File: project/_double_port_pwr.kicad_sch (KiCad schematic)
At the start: 8 parts, among them J201 RJ45_LED_Shielded_x2, U201 PCA9685PW

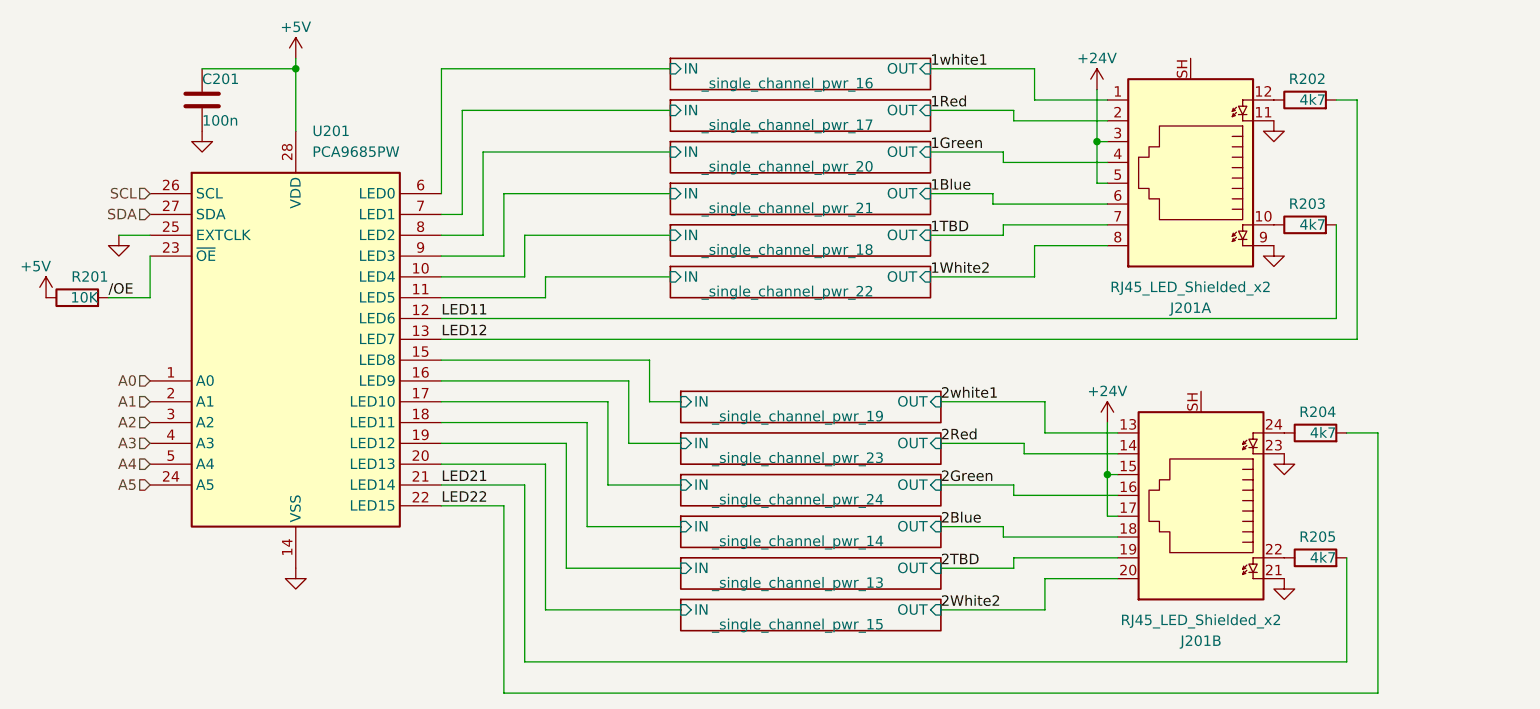
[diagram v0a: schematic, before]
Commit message: 2ch grouping layout
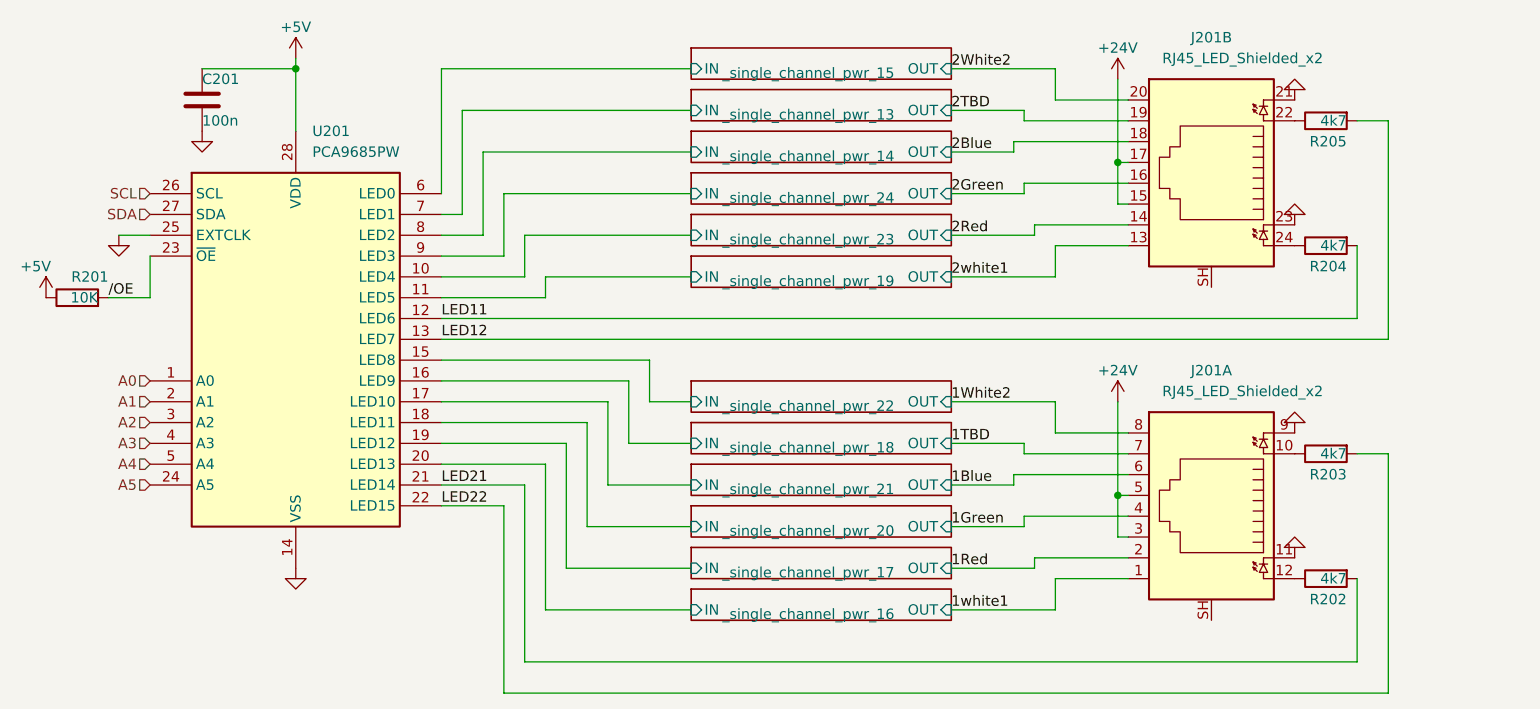
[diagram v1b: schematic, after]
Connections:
- net LED11: now also R204.2; no longer R203.2
- net LED12: now also R205.2; no longer R202.2
- net LED21: now also R202.2; no longer R205.2
- net LED22: now also R203.2; no longer R204.2
- net _single_channel_pwr_13/IN: now also U201.7 (LED1); no longer U201.19 (LED12)
- net _single_channel_pwr_14/IN: now also U201.8 (LED2); no longer U201.18 (LED11)
- net _single_channel_pwr_15/IN: now also U201.6 (LED0); no longer U201.20 (LED13)
- net _single_channel_pwr_16/IN: now also U201.20 (LED13); no longer U201.6 (LED0)
- net _single_channel_pwr_17/IN: now also U201.19 (LED12); no longer U201.7 (LED1)
- net _single_channel_pwr_18/IN: now also U201.16 (LED9); no longer U201.10 (LED4)
- net _single_channel_pwr_19/IN: now also U201.11 (LED5); no longer U201.15 (LED8)
- net _single_channel_pwr_20/IN: now also U201.18 (LED11); no longer U201.8 (LED2)
- net _single_channel_pwr_21/IN: now also U201.17 (LED10); no longer U201.9 (LED3)
- net _single_channel_pwr_22/IN: now also U201.15 (LED8); no longer U201.11 (LED5)
- net _single_channel_pwr_23/IN: now also U201.10 (LED4); no longer U201.16 (LED9)
- net _single_channel_pwr_24/IN: now also U201.9 (LED3); no longer U201.17 (LED10)
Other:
- moved on the sheet: J201A, J201B, R202, R203, R204, R205

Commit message: more layout
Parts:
- renumbered C201 to C12, J201 to J5, R204 to R10, R203 to R11, R202 to R12, R201 to R8, R205 to R9, U201 to U2
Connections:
- net GND: now also J5.SH, J5.SH
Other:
- title: (none) -> LED Dimmer 6x6
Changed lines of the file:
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@@
 (kicad_sch (version 20211123) (generator eeschema)
   (paper "A4")
+  (title_block
+    (title "LED Dimmer 6x6")
+    (date "2025-01-13")
+    (rev "1.0")
+  )
   (junction (at 191.77 118.11) (diameter 0) (color 0 0 0 0)
   )
@@
   (symbol (lib_id "-pwr:GND") (at 213.36 110.49 0) (mirror x) (unit 1)
     (in_bom yes) (on_board yes) (fields_autoplaced)
-    (property "Reference" "#PWR0209" (id 0) (at 213.36 104.14 0)
+    (property "Reference" "#PWR030" (id 0) (at 213.36 104.14 0)
       (effects (font (size 1.27 1.27)) hide)
     )
@@
     (pin "1")
   )
+  (symbol (lib_id "-pwr:GND") (at 203.2 92.71 0) (unit 1)
+    (in_bom yes) (on_board yes) (fields_autoplaced)
+    (property "Reference" "#PWR026" (id 0) (at 203.2 99.06 0)
+      (effects (font (size 1.27 1.27)) hide)
+    )
+    (property "Value" "GND" (id 1) (at 203.2 96.52 0)
+      (effects (font (size 1.27 1.27)) hide)
+    )
+    (property "Footprint" "" (id 2) (at 203.2 92.71 0)
+      (effects (font (size 1.27 1.27)) hide)
+    )
+    (property "Datasheet" "" (id 3) (at 203.2 92.71 0)
+      (effects (font (size 1.27 1.27)) hide)
+    )
+    (pin "1")
+  )
   (symbol (lib_id "-pwr:GND") (at 69.85 86.36 0) (unit 1)
     (in_bom yes) (on_board yes) (fields_autoplaced)
-    (property "Reference" "#PWR0202" (id 0) (at 69.85 92.71 0)
+    (property "Reference" "#PWR020" (id 0) (at 69.85 92.71 0)
       (effects (font (size 1.27 1.27)) hide)
     )
@@
   (symbol (lib_id "Device:R") (at 217.17 128.27 90) (mirror x) (unit 1)
     (in_bom yes) (on_board yes)
-    (property "Reference" "R202" (id 0) (at 219.71 130.81 90)
+    (property "Reference" "R12" (id 0) (at 219.71 130.81 90)
       (effects (font (size 1.27 1.27)) (justify left))
     )
@@
   (symbol (lib_id "power:+24V") (at 191.77 67.31 0) (mirror y) (unit 1)
     (in_bom yes) (on_board yes)
-    (property "Reference" "#PWR0207" (id 0) (at 191.77 71.12 0)
+    (property "Reference" "#PWR024" (id 0) (at 191.77 71.12 0)
       (effects (font (size 1.27 1.27)) hide)
     )
@@
   (symbol (lib_id "-pwr:+5V") (at 60.96 93.98 0) (unit 1)
     (in_bom yes) (on_board yes)
-    (property "Reference" "#PWR0201" (id 0) (at 60.96 97.79 0)
+    (property "Reference" "#PWR019" (id 0) (at 60.96 97.79 0)
       (effects (font (size 1.27 1.27)) hide)
     )
@@
   (symbol (lib_id "Device:R") (at 217.17 87.63 90) (mirror x) (unit 1)
     (in_bom yes) (on_board yes)
-    (property "Reference" "R204" (id 0) (at 219.71 90.17 90)
+    (property "Reference" "R10" (id 0) (at 219.71 90.17 90)
       (effects (font (size 1.27 1.27)) (justify left))
     )
@@
   (symbol (lib_id "-pwr:GND") (at 80.01 73.66 0) (unit 1)
     (in_bom yes) (on_board yes) (fields_autoplaced)
-    (property "Reference" "#PWR0203" (id 0) (at 80.01 80.01 0)
+    (property "Reference" "#PWR021" (id 0) (at 80.01 80.01 0)
       (effects (font (size 1.27 1.27)) hide)
     )
@@
   (symbol (lib_id "Device:R") (at 217.17 72.39 90) (mirror x) (unit 1)
     (in_bom yes) (on_board yes)
-    (property "Reference" "R205" (id 0) (at 219.71 74.93 90)
+    (property "Reference" "R9" (id 0) (at 219.71 74.93 90)
       (effects (font (size 1.27 1.27)) (justify left))
     )
@@
   (symbol (lib_id "Device:R") (at 217.17 113.03 90) (mirror x) (unit 1)
     (in_bom yes) (on_board yes)
-    (property "Reference" "R203" (id 0) (at 219.71 115.57 90)
+    (property "Reference" "R11" (id 0) (at 219.71 115.57 90)
       (effects (font (size 1.27 1.27)) (justify left))
     )
@@
   (symbol (lib_id "Device:C") (at 80.01 69.85 0) (unit 1)
     (in_bom yes) (on_board yes)
-    (property "Reference" "C201" (id 0) (at 80.01 67.31 0)
+    (property "Reference" "C12" (id 0) (at 80.01 67.31 0)
       (effects (font (size 1.27 1.27)) (justify left))
     )
@@
     (pin "2")
   )
+  (symbol (lib_id "-pwr:GND") (at 203.2 133.35 0) (unit 1)
+    (in_bom yes) (on_board yes) (fields_autoplaced)
+    (property "Reference" "#PWR027" (id 0) (at 203.2 139.7 0)
+      (effects (font (size 1.27 1.27)) hide)
+    )
+    (property "Value" "GND" (id 1) (at 203.2 137.16 0)
+      (effects (font (size 1.27 1.27)) hide)
+    )
+    (property "Footprint" "" (id 2) (at 203.2 133.35 0)
+      (effects (font (size 1.27 1.27)) hide)
+    )
+    (property "Datasheet" "" (id 3) (at 203.2 133.35 0)
+      (effects (font (size 1.27 1.27)) hide)
+    )
+    (pin "1")
+  )
   (symbol (lib_id "power:+24V") (at 191.77 106.68 0) (mirror y) (unit 1)
     (in_bom yes) (on_board yes)
-    (property "Reference" "#PWR0206" (id 0) (at 191.77 110.49 0)
+    (property "Reference" "#PWR025" (id 0) (at 191.77 110.49 0)
       (effects (font (size 1.27 1.27)) hide)
     )
@@
   (symbol (lib_id "-pwr:GND") (at 213.36 85.09 0) (mirror x) (unit 1)
     (in_bom yes) (on_board yes) (fields_autoplaced)
-    (property "Reference" "#PWR0210" (id 0) (at 213.36 78.74 0)
+    (property "Reference" "#PWR029" (id 0) (at 213.36 78.74 0)
       (effects (font (size 1.27 1.27)) hide)
     )
@@
   (symbol (lib_id "Driver_LED:PCA9685PW") (at 91.44 99.06 0) (unit 1)
     (in_bom yes) (on_board yes) (fields_autoplaced)
-    (property "Reference" "U201" (id 0) (at 93.4594 73.66 0)
+    (property "Reference" "U2" (id 0) (at 93.4594 73.66 0)
       (effects (font (size 1.27 1.27)) (justify left))
     )
@@
   (symbol (lib_id "-pwr:GND") (at 91.44 127 0) (unit 1)
     (in_bom yes) (on_board yes) (fields_autoplaced)
-    (property "Reference" "#PWR0205" (id 0) (at 91.44 133.35 0)
+    (property "Reference" "#PWR023" (id 0) (at 91.44 133.35 0)
       (effects (font (size 1.27 1.27)) hide)
     )
@@
   (symbol (lib_id "Device:R") (at 64.77 93.98 90) (unit 1)
     (in_bom yes) (on_board yes)
-    (property "Reference" "R201" (id 0) (at 68.58 91.44 90)
+    (property "Reference" "R8" (id 0) (at 68.58 91.44 90)
       (effects (font (size 1.27 1.27)) (justify left))
     )
@@
   (symbol (lib_id "Connector:RJ45_LED_Shielded_x2") (at 203.2 80.01 0) (mirror y) (unit 2)
     (in_bom yes) (on_board yes)
-    (property "Reference" "J201" (id 0) (at 203.2 62.23 0))
+    (property "Reference" "J5" (id 0) (at 203.2 62.23 0))
     (property "Value" "RJ45_LED_Shielded_x2" (id 1) (at 207.01 64.77 0))
     (property "Footprint" "-local:RJ45_CONNFLY-Elec_DS1129-04-S8B0P-X" (id 2) (at 203.2 79.375 90)
@@
   (symbol (lib_id "-pwr:GND") (at 213.36 125.73 0) (mirror x) (unit 1)
     (in_bom yes) (on_board yes) (fields_autoplaced)
-    (property "Reference" "#PWR0208" (id 0) (at 213.36 119.38 0)
+    (property "Reference" "#PWR031" (id 0) (at 213.36 119.38 0)
       (effects (font (size 1.27 1.27)) hide)
     )
@@
   (symbol (lib_id "-pwr:GND") (at 213.36 69.85 0) (mirror x) (unit 1)
     (in_bom yes) (on_board yes) (fields_autoplaced)
-    (property "Reference" "#PWR0211" (id 0) (at 213.36 63.5 0)
+    (property "Reference" "#PWR028" (id 0) (at 213.36 63.5 0)
       (effects (font (size 1.27 1.27)) hide)
     )
@@
   (symbol (lib_id "-pwr:+5V") (at 91.44 64.77 0) (unit 1)
     (in_bom yes) (on_board yes)
-    (property "Reference" "#PWR0204" (id 0) (at 91.44 68.58 0)
+    (property "Reference" "#PWR022" (id 0) (at 91.44 68.58 0)
       (effects (font (size 1.27 1.27)) hide)
     )
@@
   (symbol (lib_id "Connector:RJ45_LED_Shielded_x2") (at 203.2 120.65 0) (mirror y) (unit 1)
     (in_bom yes) (on_board yes)
-    (property "Reference" "J201" (id 0) (at 203.2 102.87 0))
+    (property "Reference" "J5" (id 0) (at 203.2 102.87 0))
     (property "Value" "RJ45_LED_Shielded_x2" (id 1) (at 207.01 105.41 0))
     (property "Footprint" "-local:RJ45_CONNFLY-Elec_DS1129-04-S8B0P-X" (id 2) (at 203.2 120.015 90)

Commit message: prepared for production
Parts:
- C12, J5, U2: jlc-part-type (none) -> E
- R8: value 10K -> 10k; lcsc# (none) -> C17414
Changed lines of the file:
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@@
+      (effects (font (size 1.27 1.27)) hide)
+    )
+    (property "WE" "" (id 6) (at 217.17 128.27 0)
       (effects (font (size 1.27 1.27)) hide)
     )
@@
       (effects (font (size 1.27 1.27)) hide)
     )
+    (property "WE" "" (id 6) (at 217.17 87.63 0)
+      (effects (font (size 1.27 1.27)) hide)
+    )
     (pin "1")
     (pin "2")
@@
       (effects (font (size 1.27 1.27)) hide)
     )
+    (property "WE" "" (id 6) (at 217.17 72.39 0)
+      (effects (font (size 1.27 1.27)) hide)
+    )
     (pin "1")
     (pin "2")
@@
       (effects (font (size 1.27 1.27)) hide)
     )
+    (property "WE" "" (id 6) (at 217.17 113.03 0)
+      (effects (font (size 1.27 1.27)) hide)
+    )
     (pin "1")
     (pin "2")
@@
     )
     (property "lcsc#" "C161260" (id 5) (at 80.01 69.85 0)
+      (effects (font (size 1.27 1.27)) hide)
+    )
+    (property "jlc-part-type" "E" (id 6) (at 80.01 69.85 0)
+      (effects (font (size 1.27 1.27)) hide)
+    )
+    (property "WE" "" (id 7) (at 80.01 69.85 0)
       (effects (font (size 1.27 1.27)) hide)
     )
@@
       (effects (font (size 1.27 1.27)) (justify left) hide)
     )
-    (property "Datasheet" "http://www.nxp.com/documents/data_sheet/PCA9685.pdf" (id 3) (at 81.28 81.28 0)
+    (property "Datasheet" "https://www.lcsc.com/datasheet/lcsc_datasheet_2405281434_NXP-Semicon-PCA9685PW-118_C2678753.pdf" (id 3) (at 81.28 81.28 0)
       (effects (font (size 1.27 1.27)) hide)
     )
     (property "lcsc#" "C2678753" (id 4) (at 91.44 99.06 0)
+      (effects (font (size 1.27 1.27)) hide)
+    )
+    (property "jlc-part-type" "E" (id 5) (at 91.44 99.06 0)
+      (effects (font (size 1.27 1.27)) hide)
+    )
+    (property "WE" "" (id 6) (at 91.44 99.06 0)
       (effects (font (size 1.27 1.27)) hide)
     )
@@
       (effects (font (size 1.27 1.27)) (justify left))
     )
-    (property "Value" "10K" (id 1) (at 67.31 93.98 90)
+    (property "Value" "10k" (id 1) (at 67.31 93.98 90)
       (effects (font (size 1.27 1.27)) (justify left))
     )
@@
       (effects (font (size 1.27 1.27)) hide)
     )
-    (property "lcsc#" "" (id 5) (at 64.77 93.98 0)
+    (property "lcsc#" "C17414" (id 5) (at 64.77 93.98 0)
+      (effects (font (size 1.27 1.27)) hide)
+    )
+    (property "WE" "" (id 6) (at 64.77 93.98 0)
       (effects (font (size 1.27 1.27)) hide)
     )
@@
     )
     (property "lcsc#" "C86581" (id 4) (at 203.2 80.01 0)
+      (effects (font (size 1.27 1.27)) hide)
+    )
+    (property "jlc-part-type" "E" (id 5) (at 203.2 80.01 0)
+      (effects (font (size 1.27 1.27)) hide)
+    )
+    (property "WE" "" (id 6) (at 203.2 80.01 0)
       (effects (font (size 1.27 1.27)) hide)
     )
@@
       (effects (font (size 1.27 1.27)) hide)
     )
+    (property "jlc-part-type" "E" (id 5) (at 203.2 120.65 0)
+      (effects (font (size 1.27 1.27)) hide)
+    )
+    (property "WE" "" (id 6) (at 203.2 120.65 0)
+      (effects (font (size 1.27 1.27)) hide)
+    )

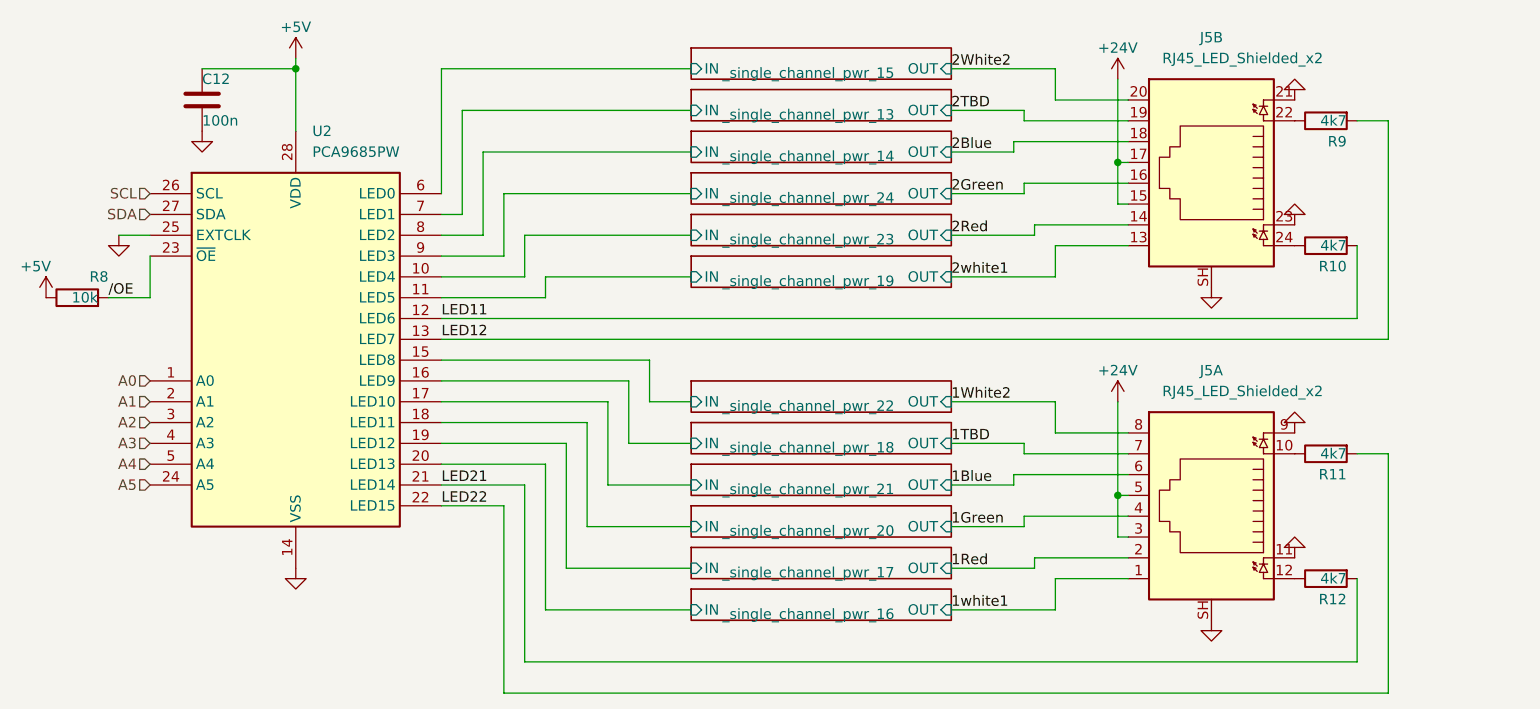
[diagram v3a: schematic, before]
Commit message: improvements after first prototype test
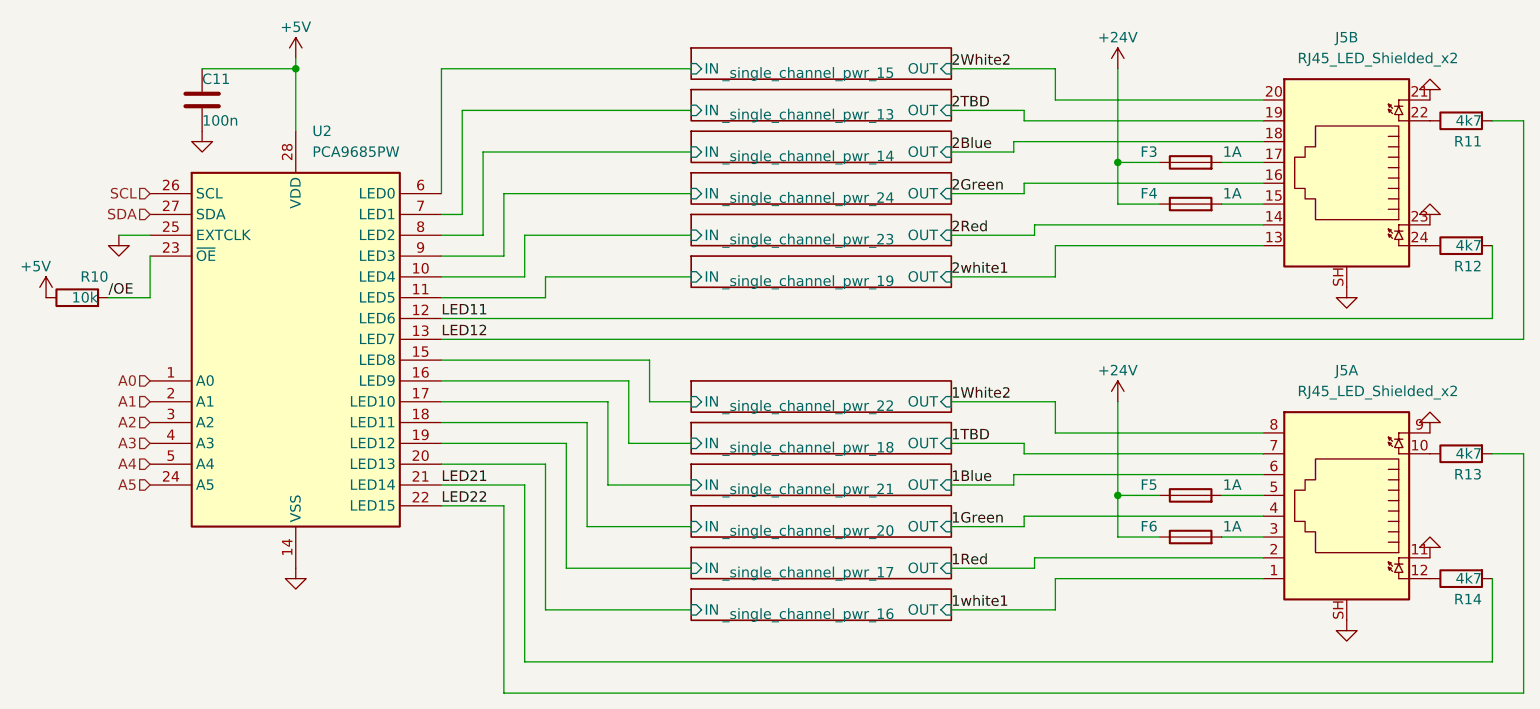
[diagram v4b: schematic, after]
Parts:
- added F3, F4, F5, F6: 1A, Fuse:Fuse_1206_3216Metric_Pad1.42x1.75mm_HandSolder, symbol Device:Fuse
- C11: renamed from C12; jlc-part-type E -> B; lcsc# C161260 -> C49678
- renumbered R8 to R10, R9 to R11, R10 to R12, R11 to R13, R12 to R14
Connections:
- net +24V: now also F3.1, F4.1, F5.1, F6.1; no longer J5.15, J5.17, J5.3, J5.5
- new net: F5.2, J5.5
- new net: F4.2, J5.15
- new net: F3.2, J5.17
- new net: F6.2, J5.3
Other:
- title: LED Dimmer 6x6 -> LED_Dimmer_6x6
- moved on the sheet: J5A, J5B, R11, R12, R13, R14
